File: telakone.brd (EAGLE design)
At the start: 100 x 100 mm, 189 parts, among them X10 MPT0.5/8-2.54, X11 MPT0.5/8-2.54, X2 MPT0.5/8-2.54, X3 MPT0.5/8-2.54, X4 PIIKKIRIMA-2, X5 PIIKKIRIMA-5, X7 U.FL-R-SMT-1, X8 MPT0.5/8-2.54, X9 PIIKKIRIMA-3, Y1 PTH2.6-5.5SQ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

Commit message: small fixes
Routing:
- net +12V: track 225.4 -> 215.1 mm
- net I2C1SCL: track 41.3 -> 40.1 mm
- net GND: vias 229 -> 260
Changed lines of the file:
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@@
 <layer number="17" name="Pads" color="2" fill="1" visible="yes" active="yes"/>
 <layer number="18" name="Vias" color="2" fill="1" visible="yes" active="yes"/>
-<layer number="19" name="Unrouted" color="6" fill="1" visible="no" active="yes"/>
+<layer number="19" name="Unrouted" color="6" fill="1" visible="yes" active="yes"/>
 <layer number="20" name="Dimension" color="15" fill="1" visible="no" active="yes"/>
 <layer number="21" name="tPlace" color="7" fill="1" visible="yes" active="yes"/>
@@
 </element>
 <element name="C24" library="omat_ic_2" package="C0603" value="" x="58.599603125" y="28.14139375" smashed="yes" rot="R45">
-<attribute name="NAME" x="57.351575" y="27.94139375" size="0.8128" layer="25" rot="R45"/>
+<attribute name="NAME" x="56.151575" y="28.14139375" size="0.8128" layer="25" rot="R45"/>
 <attribute name="VALUE" x="59.497628125" y="26.345340625" size="0.8128" layer="27" rot="R45"/>
 </element>
@@
 </element>
 <element name="D11" library="omat_ic_2" package="SOIC8-N_MC" value="LM75BD" x="33.782" y="7.493" smashed="yes" rot="R270">
-<attribute name="NAME" x="36.4044" y="7.676" size="0.8128" layer="25" ratio="10" rot="SR0"/>
+<attribute name="NAME" x="36.4544" y="7.026" size="0.8128" layer="25" ratio="10" rot="SR0"/>
 <attribute name="VALUE" x="30.3276" y="9.2202" size="0.8128" layer="27" ratio="10" rot="SR270"/>
 </element>
@@
 <via x="98.969" y="27.983" extent="1-16" drill="0.5"/>
 <via x="99.069" y="34.183" extent="1-16" drill="0.5"/>
+<via x="69.372" y="83.873" extent="1-16" drill="0.5"/>
+<via x="72.222" y="78.073" extent="1-16" drill="0.5"/>
+<via x="84.672" y="85.323" extent="1-16" drill="0.5"/>
+<via x="85.272" y="84.523" extent="1-16" drill="0.5"/>
+<via x="85.572" y="83.473" extent="1-16" drill="0.5"/>
+<via x="85.622" y="82.273" extent="1-16" drill="0.5"/>
+<via x="86.156" y="69.164" extent="1-16" drill="0.5"/>
+<via x="60.952" y="78.253" extent="1-16" drill="0.5"/>
+<via x="60.952" y="77.353" extent="1-16" drill="0.5"/>
+<via x="60.902" y="81.703" extent="1-16" drill="0.5"/>
+<via x="70.372" y="84.823" extent="1-16" drill="0.5"/>
+<via x="70.372" y="85.773" extent="1-16" drill="0.5"/>
+<via x="70.372" y="86.723" extent="1-16" drill="0.5"/>
+<via x="66.672" y="75.723" extent="1-16" drill="0.5"/>
+<via x="72.122" y="55.323" extent="1-16" drill="0.5"/>
+<via x="72.872" y="56.173" extent="1-16" drill="0.5"/>
+<via x="80.272" y="55.723" extent="1-16" drill="0.5"/>
+<via x="61.022" y="50.823" extent="1-16" drill="0.5"/>
+<via x="48.672" y="59.673" extent="1-16" drill="0.5"/>
+<via x="52.722" y="57.023" extent="1-16" drill="0.5"/>
+<via x="42.272" y="45.023" extent="1-16" drill="0.5"/>
+<via x="44.822" y="47.523" extent="1-16" drill="0.5"/>
+<via x="58.272" y="31.073" extent="1-16" drill="0.5"/>
+<via x="54.822" y="27.423" extent="1-16" drill="0.5"/>
+<via x="57.972" y="29.273" extent="1-16" drill="0.5"/>
+<via x="52.593" y="23.835" extent="1-16" drill="0.5"/>
+<via x="53.293" y="14.285" extent="1-16" drill="0.5"/>
+<via x="57.093" y="13.285" extent="1-16" drill="0.5"/>
+<via x="14.543" y="6.085" extent="1-16" drill="0.5"/>
+<via x="14.543" y="7.635" extent="1-16" drill="0.5"/>
+<via x="30.132" y="5.054" extent="1-16" drill="0.5"/>
 </signal>
 <signal name="N$4">
@@
 <wire x1="47.371" y1="54.991" x2="33.528" y2="54.991" width="1" layer="16"/>
 <wire x1="20" y1="18.25" x2="21.552" y2="18.25" width="0.5" layer="1"/>
-<wire x1="21.552" y1="18.25" x2="21.59" y2="18.288" width="0.5" layer="1"/>
-<via x="21.59" y="18.288" extent="1-16" drill="0.5"/>
-<wire x1="21.59" y1="18.288" x2="23.368" y2="18.288" width="0.5" layer="16"/>
+<wire x1="21.552" y1="18.25" x2="22.79" y2="18.238" width="0.5" layer="1"/>
+<via x="22.79" y="18.238" extent="1-16" drill="0.5"/>
+<wire x1="22.79" y1="18.238" x2="23.368" y2="18.288" width="0.5" layer="16"/>
 <wire x1="22.86" y1="6.87" x2="23.634" y2="6.87" width="0.5" layer="1"/>
-<wire x1="23.634" y1="6.87" x2="24.257" y2="7.493" width="0.5" layer="1"/>
-<via x="24.257" y="7.493" extent="1-16" drill="0.5"/>
-<wire x1="24.257" y1="7.493" x2="25.654" y2="8.89" width="0.5" layer="16"/>
+<wire x1="23.634" y1="6.87" x2="25.657" y2="8.893" width="0.5" layer="1"/>
+<via x="25.657" y="8.893" extent="1-16" drill="0.5"/>
+<wire x1="25.657" y1="8.893" x2="25.654" y2="8.89" width="0.5" layer="16"/>
 <wire x1="15.7988" y1="6.858" x2="13.462" y2="6.858" width="0.3" layer="1"/>
 <wire x1="13.462" y1="6.858" x2="13.462" y2="11.176" width="0.5" layer="1"/>
 <wire x1="13.462" y1="11.176" x2="14.351" y2="12.065" width="0.5" layer="1"/>
-<wire x1="14.351" y1="12.065" x2="20.574" y2="12.065" width="0.5" layer="1"/>
-<wire x1="20.574" y1="12.065" x2="21.336" y2="12.827" width="0.5" layer="1"/>
-<via x="21.336" y="12.827" extent="1-16" drill="0.5"/>
-<wire x1="21.336" y1="12.827" x2="23.241" y2="12.827" width="0.5" layer="16"/>
+<wire x1="14.351" y1="12.065" x2="20.815" y2="12.065" width="0.5" layer="1"/>
+<wire x1="20.815" y1="12.065" x2="21.55" y2="12.8" width="0.5" layer="1"/>
+<wire x1="21.55" y1="12.8" x2="23.2" y2="12.8" width="0.5" layer="1"/>
+<wire x1="23.2" y1="12.8" x2="23.25" y2="12.85" width="0.5" layer="1"/>
+<wire x1="23.25" y1="12.8" x2="23.25" y2="12.85" width="0.5" layer="1"/>
+<wire x1="23.25" y1="12.85" x2="23.236" y2="12.827" width="0.5" layer="1"/>
+<via x="23.236" y="12.827" extent="1-16" drill="0.5"/>
+<wire x1="23.236" y1="12.827" x2="23.241" y2="12.827" width="0.5" layer="16"/>
 <wire x1="23.241" y1="12.827" x2="23.368" y2="12.7" width="0.5" layer="16"/>
-<wire x1="37.084" y1="5.195" x2="37.084" y2="6.477" width="0.5" layer="1"/>
-<via x="37.084" y="6.477" extent="1-16" drill="0.5"/>
-<wire x1="37.084" y1="6.477" x2="37.084" y2="8.636" width="0.5" layer="16"/>
+<wire x1="37.084" y1="5.195" x2="37.084" y2="8.677" width="0.5" layer="1"/>
+<via x="37.084" y="8.677" extent="1-16" drill="0.5"/>
+<wire x1="37.084" y1="8.677" x2="37.084" y2="8.636" width="0.5" layer="16"/>
 <wire x1="37.084" y1="5.195" x2="35.7512" y2="5.195" width="0.5" layer="1"/>
 <wire x1="35.7512" y1="5.195" x2="35.687" y2="5.1308" width="0.5" layer="1"/>
@@
 <wire x1="37.428" y1="11.52" x2="37.338" y2="11.43" width="0.5" layer="1"/>
 <via x="37.338" y="11.43" extent="1-16" drill="0.5"/>
-<wire x1="37.338" y1="11.43" x2="37.338" y2="8.509" width="0.5" layer="16"/>
+<wire x1="37.338" y1="11.43" x2="37.338" y2="8.509" width="1" layer="16"/>
 <wire x1="39.751" y1="17.399" x2="39.751" y2="13.843" width="0.5" layer="16"/>
 <wire x1="39.751" y1="13.843" x2="37.338" y2="11.43" width="0.5" layer="16"/>
@@
 <wire x1="15.47" y1="31.98" x2="15.494" y2="32.004" width="0.3" layer="1"/>
 <via x="15.494" y="32.004" extent="1-16" drill="0.5"/>
-<wire x1="15.494" y1="32.004" x2="17.526" y2="32.004" width="0.5" layer="16"/>
+<wire x1="15.494" y1="32.004" x2="17.526" y2="32.004" width="2" layer="16"/>
 <wire x1="33.516" y1="59.817" x2="33.516" y2="55.003" width="0.5" layer="1"/>
 <wire x1="33.516" y1="55.003" x2="33.528" y2="54.991" width="0.5" layer="1"/>
@@
 <wire x1="76.215" y1="80.715" x2="75.5" y2="80" width="0.3" layer="1"/>
 <wire x1="85.09" y1="80" x2="87.56" y2="77.53" width="2" layer="16"/>
-<wire x1="87.56" y1="77.53" x2="97.86" y2="77.53" width="2" layer="16"/>
 <wire x1="97.86" y1="77.53" x2="87.53" y2="77.53" width="2" layer="1"/>
 <wire x1="87.53" y1="77.53" x2="87.5" y2="77.5" width="2" layer="1"/>
@@
 <wire x1="3.75" y1="48.25" x2="3.76" y2="48.26" width="0.3" layer="1"/>
 <wire x1="3.76" y1="48.26" x2="3.81" y2="48.26" width="0.3" layer="1"/>
+<wire x1="87.56" y1="77.53" x2="87.53" y2="77.53" width="0" layer="19" extent="1-1"/>
 </signal>
 <signal name="N$11">
@@
 <wire x1="34.417" y1="9.8552" x2="34.417" y2="9.779" width="0.3" layer="1"/>
 <wire x1="34.417" y1="9.8552" x2="34.417" y2="8.509" width="0.3" layer="1"/>
-<wire x1="34.417" y1="8.509" x2="34.036" y2="8.128" width="0.3" layer="1"/>
-<wire x1="34.036" y1="8.128" x2="26.035" y2="8.128" width="0.3" layer="1"/>
-<wire x1="26.035" y1="8.128" x2="25.019" y2="7.112" width="0.3" layer="1"/>
-<wire x1="25.019" y1="7.112" x2="25.019" y2="5.207" width="0.3" layer="1"/>
-<wire x1="25.019" y1="5.207" x2="24.384" y2="4.572" width="0.3" layer="1"/>
-<wire x1="24.384" y1="4.572" x2="18.796" y2="4.572" width="0.3" layer="1"/>
+<wire x1="34.417" y1="8.509" x2="34.054" y2="8.146" width="0.3" layer="1"/>
+<wire x1="27.722" y1="4.572" x2="18.796" y2="4.572" width="0.3" layer="1"/>
 <wire x1="18.542" y1="5.6388" x2="18.542" y2="4.826" width="0.3" layer="1"/>
 <wire x1="18.542" y1="4.826" x2="18.796" y2="4.572" width="0.3" layer="1"/>
+<wire x1="27.722" y1="4.572" x2="31.25" y2="8.1" width="0.3" layer="1"/>
+<wire x1="31.25" y1="8.1" x2="34.008" y2="8.1" width="0.3" layer="1"/>
+<wire x1="34.008" y1="8.1" x2="34.036" y2="8.128" width="0.3" layer="1"/>
+<wire x1="34.054" y1="8.146" x2="34.036" y2="8.128" width="0.3" layer="1"/>
 </signal>
 <signal name="I2C1SDA">
@@
 <wire x1="50.45" y1="43.25" x2="55.2" y2="48" width="0.3" layer="16"/>
 <wire x1="55.2" y1="48" x2="68.45" y2="48" width="0.3" layer="16"/>
-<wire x1="71" y1="47.4" x2="70.5" y2="47.4" width="0" layer="19" extent="1-16"/>
 <via x="70.5" y="47.4" extent="1-16" drill="0.5"/>
 <wire x1="70.5" y1="47.4" x2="71.4" y2="47.4" width="0.3" layer="1"/>

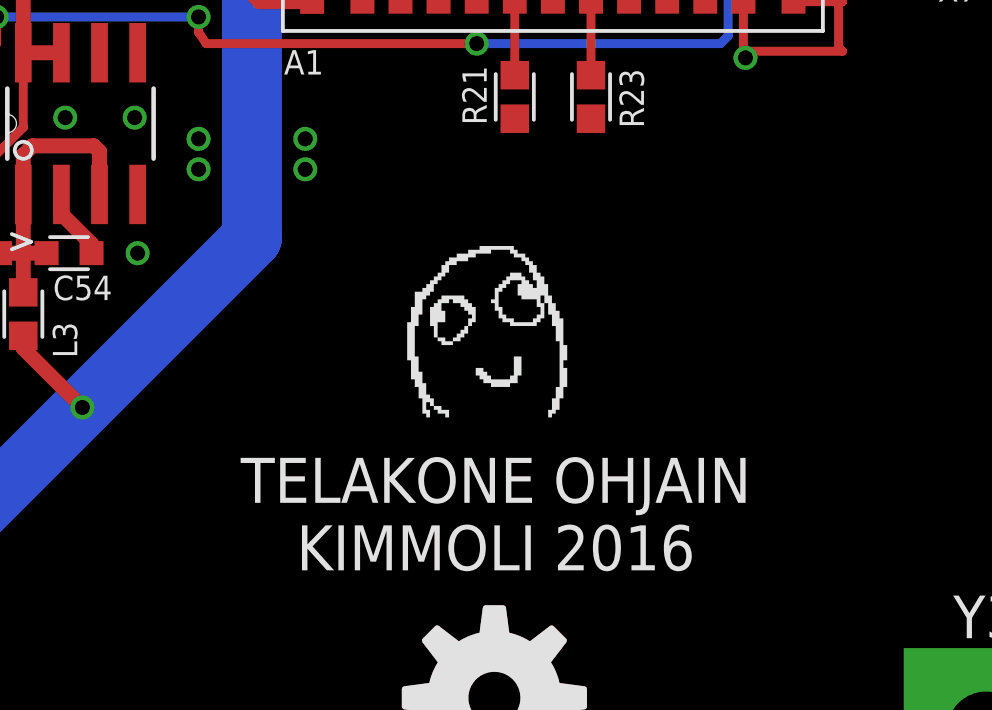
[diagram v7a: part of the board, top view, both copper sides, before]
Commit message: add version label to board
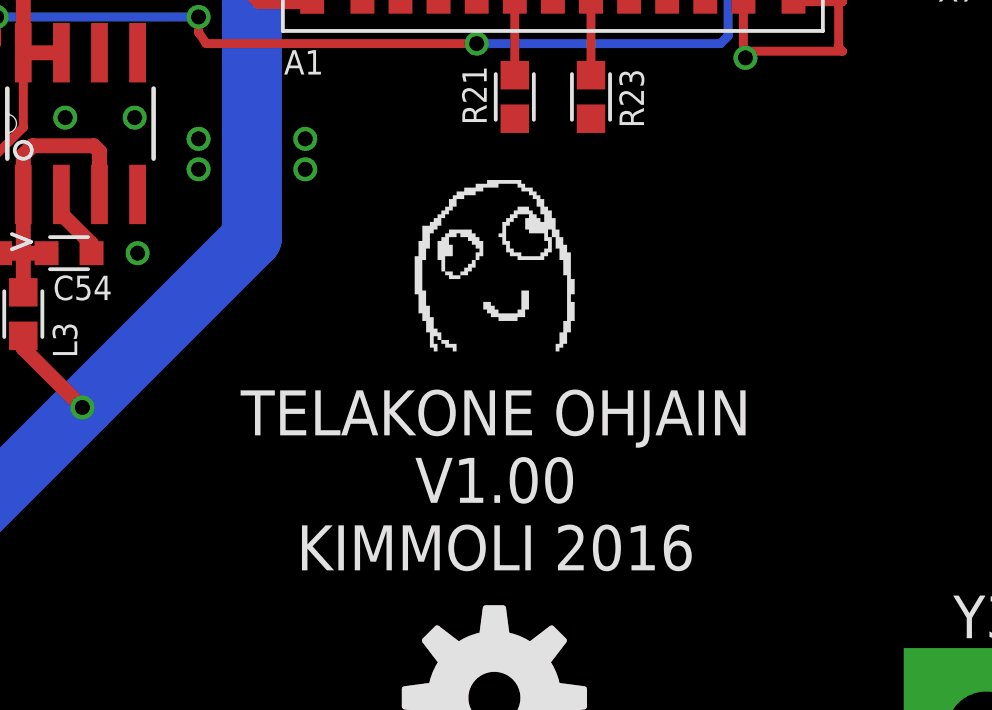
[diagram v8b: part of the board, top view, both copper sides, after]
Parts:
- moved U$1 2.21 mm to (80.8, 18.2)
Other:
- board text added: "TELAKONE OHJAIN V1.00 KIMMOLI 2016"
- board text removed: "TELAKONE OHJAIN KIMMOLI 2016"
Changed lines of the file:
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@@
 <wire x1="74.55" y1="27.3" x2="74.55" y2="46.35" width="2" layer="41"/>
 <text x="80.65" y="8.35" size="1.5" layer="21" align="bottom-center">TELAKONE OHJAIN
+V1.00
 KIMMOLI 2016</text>
 <text x="50" y="1" size="1.5" layer="21" align="bottom-center">https://github.com/kimmoli/telakone-controller</text>
@@
 <attribute name="VALUE" x="51.305" y="8.865" size="0.8128" layer="27" rot="R90"/>
 </element>
-<element name="U$1" library="dafug" package="DAFUG" value="DAFUG" x="80.55" y="16.05" smashed="yes"/>
+<element name="U$1" library="dafug" package="DAFUG" value="DAFUG" x="80.8" y="18.25" smashed="yes"/>
 <element name="Y5" library="EKE" package="PTH-2.6-5.5SQ" value="PTH2.6-5.5SQ" x="60" y="60"/>
 </elements>
